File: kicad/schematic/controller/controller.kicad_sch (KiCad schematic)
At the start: 77 parts, among them J5 SMA, SW1 SW_Push, SW3 SW_SPDT, SW4 SW_Push, SW5 SW_Push, U1 ATmega328P, U10 Joystick, U2 NRF24L01, U3 RFX2401C, U4 ILI9341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

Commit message: controller schematics updated
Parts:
- removed C10: 4.7nF, symbol common:Capacitor
- removed C11, C16, C17, C18, C19: 1.5pF, symbol common:Capacitor
- removed C12: 1.0pF, symbol common:Capacitor
- removed C13: 220pF, symbol common:Capacitor
- removed C14: 1uF, symbol common:Capacitor
- removed C15: 0.3pF, symbol common:Capacitor
- removed C4, C5: 22pF, symbol common:Capacitor
- removed C6: 1nF, symbol common:Capacitor
- removed C7: 10nF, symbol common:Capacitor
- removed C8: F, symbol common:Capacitor
- removed C9: 2.2nF, symbol common:Capacitor
- removed J3: ~, symbol connector:Pin_01x06
- removed J4: ~, symbol connector:Pin_01x02
- removed J5: SMA, symbol connector:SMA
- removed L1: 8.2nH, symbol common:Inductor
- removed L2: 2.7nH, symbol common:Inductor
- removed L3: 3.9nH, symbol common:Inductor
- removed L4, L5: 2.4nH, symbol common:Inductor
- removed R1: 1M, symbol common:Resistor
- removed R10, R3, R5, R6, R7, R8, R9: 1k, symbol common:Resistor
- removed R11, R12, R13, R14, R15: 2k, symbol common:Resistor
- removed R2: 22k, symbol common:Resistor
- removed R4: 20k, symbol common:Resistor
- removed U2: NRF24L01, symbol transceiver:NRF24L01
- removed U3: RFX2401C, symbol transceiver:RFX2401C
- removed U4: ILI9341, symbol display:ILI9341
- removed Y2: Hz, symbol common:Crystal_4Pins
- added J5: ~, symbol connector:Pin_01x06
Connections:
- net +5V: now also J5.1
- net DTR: now also J5.6
- net GND: now also J5.2
- net MISO: now also J5.4
- net MOSI: now also J5.5
- net SCK: now also J5.3
- no-connect marks 5 -> 0
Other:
- added sheet Display (display.kicad_sch)
- added sheet Transceiver (transceiver.kicad_sch)
- note added: "CE missing ?"

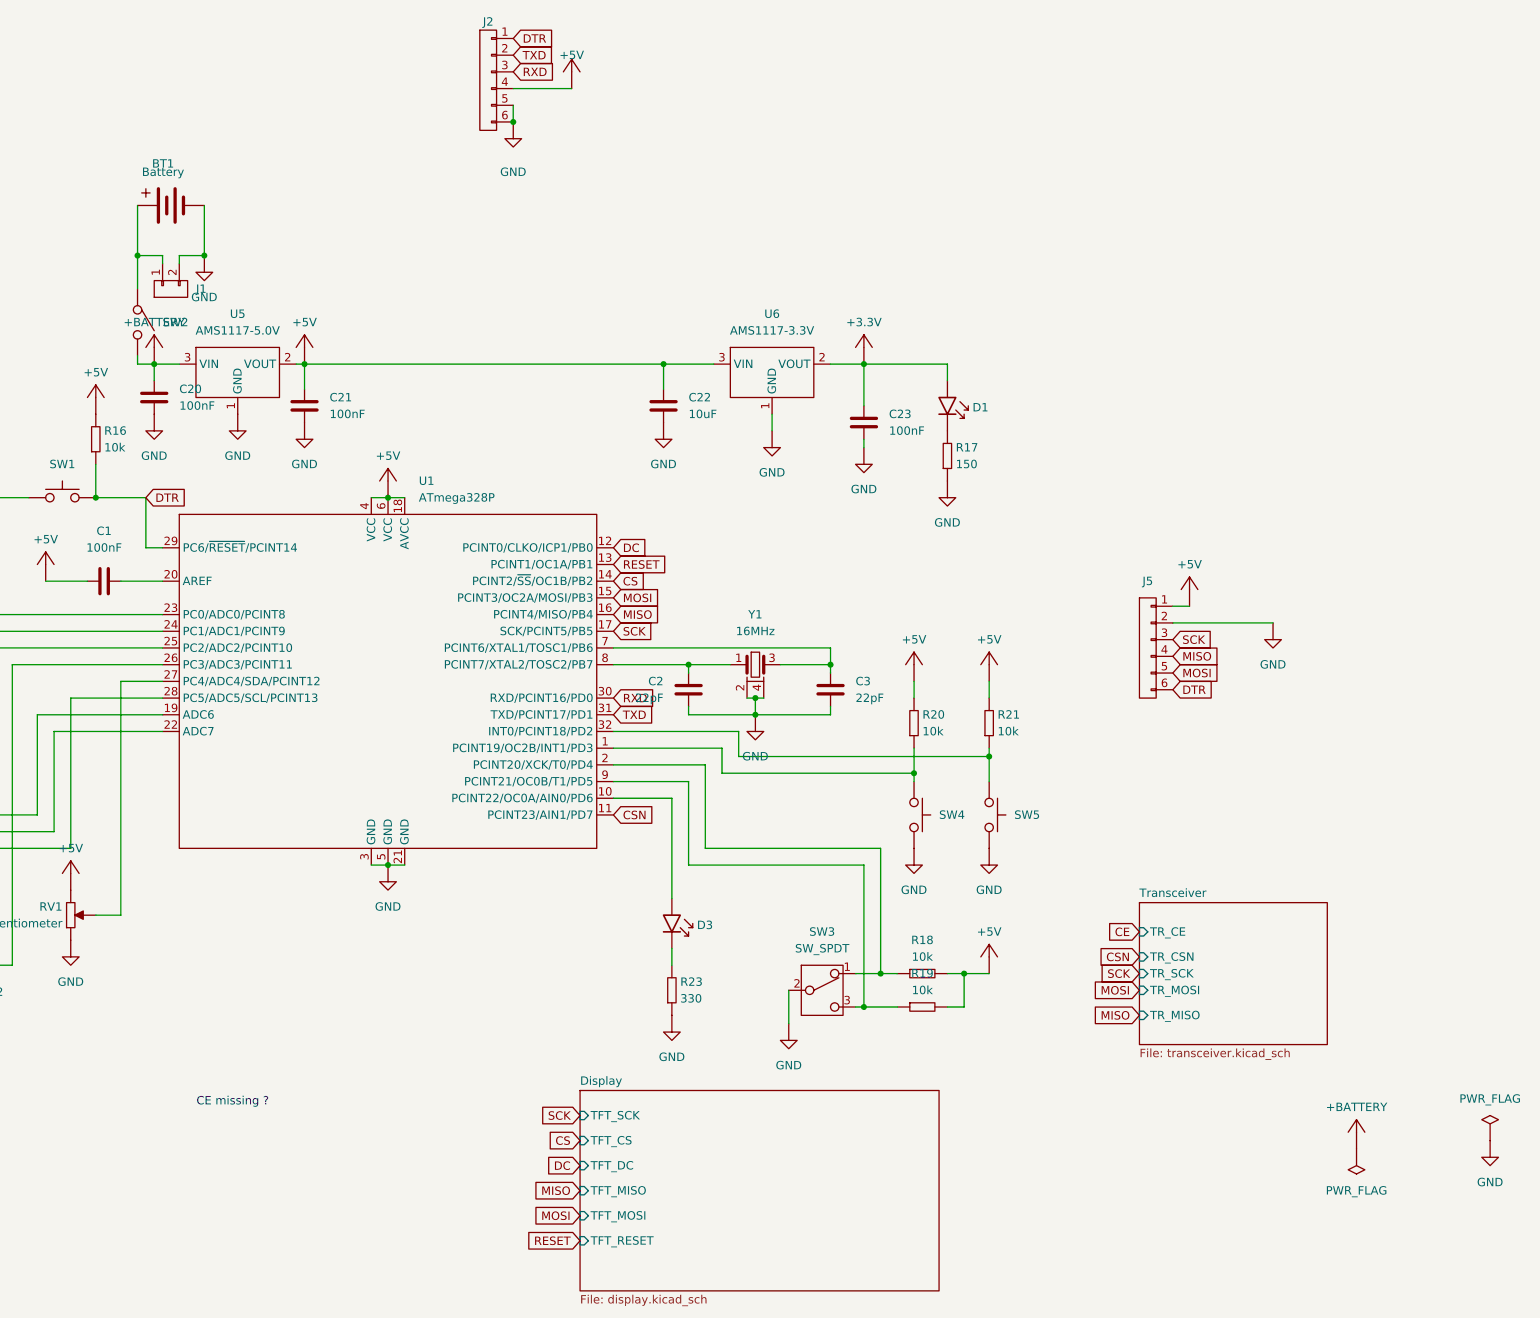
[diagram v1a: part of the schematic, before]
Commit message: fix(controller): tag CE <-> PD6
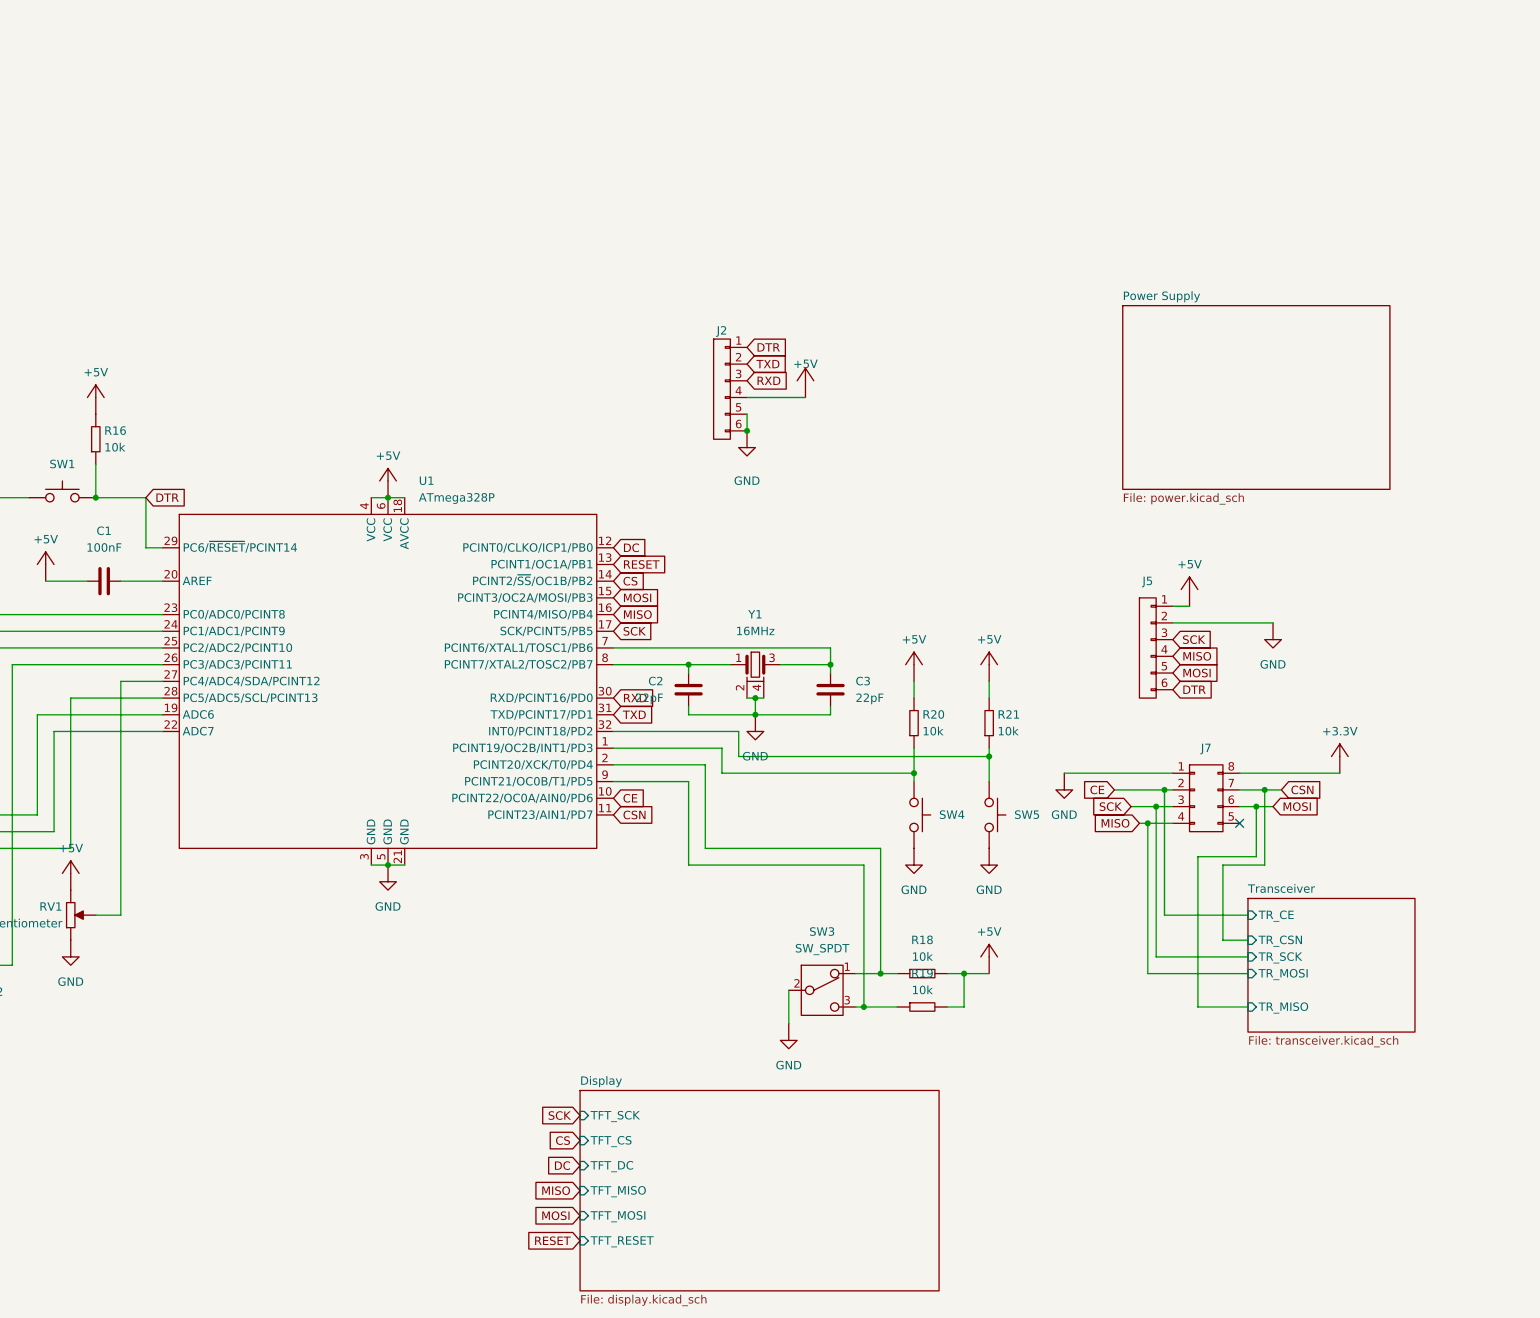
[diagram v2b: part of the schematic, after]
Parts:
- removed BT1: Battery, symbol common:Battery
- removed C20, C21, C23: 100nF, symbol common:Capacitor
- removed C22: 10uF, symbol common:Capacitor
- removed D1, D3: ~, symbol common:LED
- removed J1: ~, symbol connector:Pin_01x02
- removed R17: 150, symbol common:Resistor
- removed R23: 330, symbol common:Resistor
- removed SW2: ~, symbol common:Switch
- removed U5: AMS1117-5.0V, symbol regulator:AMS1117
- removed U6: AMS1117-3.3V, symbol regulator:AMS1117
- added J7: 02x04, connector:Pin_02x04, symbol connector:Pin_02x04
- C1, C2, C24, C3: footprint (none) -> common:C_0603
- D2: footprint (none) -> common:LED_0603
- J2, J5: value ~ -> 01x06
- R16, R18, R19, R20, R21, R22: footprint (none) -> common:R_0603
- U1: footprint (none) -> microchip:ATmega328p_TQFP
- U10, U9: footprint (none) -> misc:Joystick
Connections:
- net +3.3V: now also J7.8
- net CE: now also U1.10 (PCINT22/OC0A/AIN0/PD6), J7.2
- net CSN: now also J7.7
- net GND: now also J7.1
- net MISO: now also J7.4
- net MOSI: now also J7.6
- net SCK: now also J7.3
- no-connect marks 0 -> 1
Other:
- added sheet Power Supply (power.kicad_sch)
- note removed: "CE missing ?"
- moved on the sheet: J2

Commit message: feat(pcb): pcb wip
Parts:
- J2, J5: footprint (none) -> connector:Pin_01x06
- RV1: footprint (none) -> common:RV_45
- SW1: value SW_Push -> Reset; footprint (none) -> common:SW_Tactile06x06
- SW3: footprint (none) -> common:SW_Toggle
- SW4, SW5: footprint (none) -> common:SW_Tactile12x12
- Y1: footprint (none) -> common:Crystal_3225
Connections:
- net DTR: now also SW1.3; no longer SW1.2
- net GND: now also SW4.3, SW5.3; no longer SW4.2, SW5.2
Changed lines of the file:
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@@
 			)
 		)
-		(property "Footprint" ""
+		(property "Footprint" "common:SW_Tactile12x12"
 			(at 176.53 99.06 0)
 			(effects
@@
 			)
 		)
-		(pin "2"
+		(pin "3"
 		)
 		(pin "1"
@@
 			)
 		)
-		(property "Value" "SW_Push"
+		(property "Value" "Reset"
 			(at 35.56 52.8 0)
 			(effects
@@
 			)
 		)
-		(property "Footprint" ""
+		(property "Footprint" "common:SW_Tactile06x06"
 			(at 35.56 50.8 0)
 			(effects
@@
 			)
 		)
-		(pin "2"
+		(pin "3"
 		)
 		(pin "1"
@@
 			)
 		)
-		(property "Footprint" ""
+		(property "Footprint" "connector:Pin_01x06"
 			(at 135.89 34.29 0)
 			(effects
@@
 			)
 		)
-		(property "Footprint" ""
+		(property "Footprint" "connector:Pin_01x06"
 			(at 200.66 73.66 0)
 			(effects
@@
 			)
 		)
-		(property "Footprint" ""
+		(property "Footprint" "common:SW_Toggle"
 			(at 151.13 125.73 0)
 			(effects
@@
 			)
 		)
-		(property "Footprint" ""
+		(property "Footprint" "common:SW_Tactile12x12"
 			(at 165.1 99.06 0)
 			(effects
@@
 		(pin "1"
 		)
-		(pin "2"
+		(pin "3"
 		)
 		(instances
@@
 			)
 		)
-		(property "Footprint" ""
+		(property "Footprint" "common:RV_45"
 			(at 36.83 114.3 0)
 			(effects
@@
 			)
 		)
-		(property "Footprint" ""
+		(property "Footprint" "common:Crystal_3225"
 			(at 140.97 76.2 0)
 			(effects

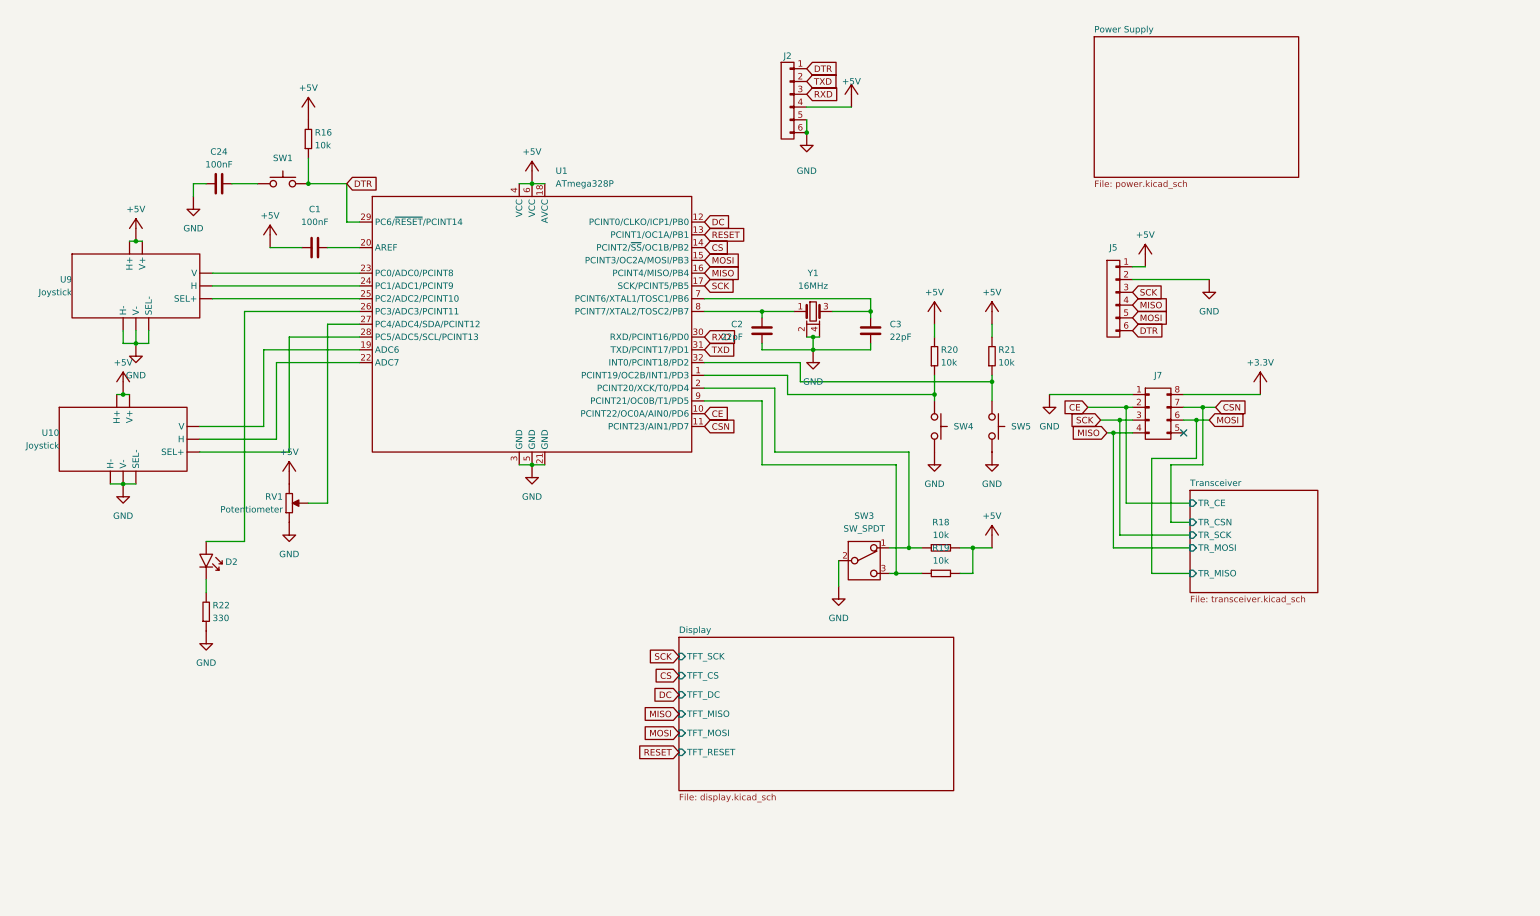
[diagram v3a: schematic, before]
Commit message: feat(schematic): cleanup controller
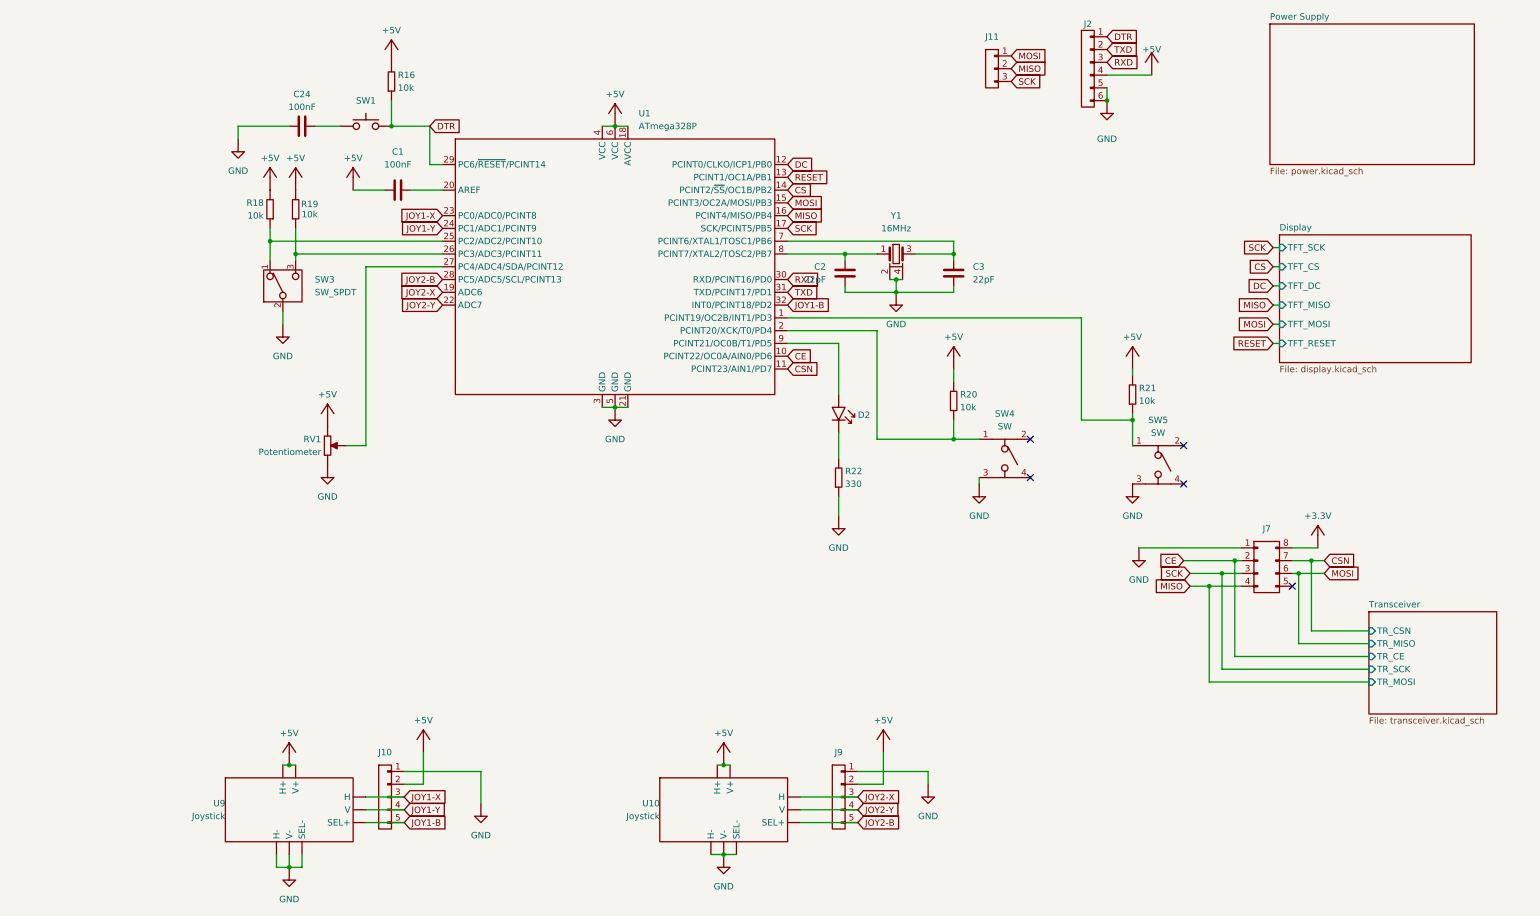
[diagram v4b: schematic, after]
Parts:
- removed J5: 01x06, connector:Pin_01x06, symbol connector:Pin_01x06
- removed SW4, SW5: SW_Push, common:SW_Tactile12x12, symbol common:SW_Push
- added J10, J9: 01x05, connector:Pin_01x05, symbol connector:Pin_01x05
- added J11: 01x03, connector:Pin_01x03, symbol connector:Pin_01x03
- added SW4, SW5: SW, switch:SW_Tactile12x12, symbol common:SW_DPST
- SW1: footprint common:SW_Tactile06x06 -> switch:SW_Tactile3x2.5
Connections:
- net +5V: now also U10.H3 (H+), U10.V3 (V+), U9.H3 (H+), U9.V3 (V+), J10.2, J9.2; no longer U10.3 (H+), U10.6 (V+), U9.3 (H+), U9.6 (V+)
- net DTR: now also SW1.2; no longer SW1.3
- net GND: now also U10.B1A (SEL-), U10.H1 (H-), U10.V1 (V-), U9.B1A (SEL-), U9.H1 (H-), U9.V1 (V-), J10.1, J9.1, SW4.3, SW5.3; no longer U10.1 (H-), U10.4 (V-), U10.7 (SEL-), U9.1 (H-), U9.4 (V-), U9.7 (SEL-)
- net MISO: now also J11.2
- net MOSI: now also J11.1
- net SCK: now also J11.3
- net at R21.1: now also U1.1 (PCINT19/OC2B/INT1/PD3), SW5.1; no longer U1.32 (INT0/PCINT18/PD2)
- net at D2.2 (A): now also U1.9 (PCINT21/OC0B/T1/PD5); no longer U1.26 (PC3/ADC3/PCINT11)
- net JOY1-Y: now reaches U1.24 (PC1/ADC1/PCINT9)
- net JOY1-Y: now also U9.V2 (V), J10.4; no longer U9.2 (H)
- net JOY1-X: now reaches U1.23 (PC0/ADC0/PCINT8)
- net JOY1-X: now also U9.H2 (H), J10.3; no longer U9.5 (V)
- net at U1.25 (PC2/ADC2/PCINT10): now also R18.1, SW3.1; no longer U9.8 (SEL+)
- net JOY2-Y: now reaches U1.22 (ADC7)
- net JOY2-Y: now also U10.V2 (V), J9.4; no longer U10.2 (H)
- net JOY2-X: now reaches U1.19 (ADC6)
- net JOY2-X: now also U10.H2 (H), J9.3; no longer U10.5 (V)
- net JOY2-B: now reaches U1.28 (PC5/ADC5/SCL/PCINT13)
- net JOY2-B: now also U10.B2A (SEL+), J9.5; no longer U10.8 (SEL+)
- net at R20.1: now also U1.2 (PCINT20/XCK/T0/PD4), SW4.1; no longer U1.1 (PCINT19/OC2B/INT1/PD3)
- net at R19.1, SW3.3: now also U1.26 (PC3/ADC3/PCINT11); no longer U1.9 (PCINT21/OC0B/T1/PD5)
- new net JOY1-B: J10.5, U1.32 (INT0/PCINT18/PD2), U9.B2A (SEL+)
- no-connect marks 1 -> 5
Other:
- moved on the sheet: C1, C2, C24, C3, D2, J2, J7, R16, R18, R19, R20, R21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
